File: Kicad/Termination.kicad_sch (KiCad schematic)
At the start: 29 parts, among them J1 Conn_02x25_Odd_Even, J5 Conn_02x25_Odd_Even, SW1 219-8MST, U11 DS21S07A, U12 DS21S07A, U8 SN74F244DB

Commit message: Add correct footprints for DIP resistors
And start adding LCSC part numbers
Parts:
- C1102, C1202: LCSC Part # (none) -> C7189
- J1, J5: LCSC Part # (none) -> C7494769
- R1, R2: footprint kicad-official/Resistor_SMD.pretty:R_0603_1608Metric_Pad0.98x0.95mm_HandSolder -> Resistor_SMD:R_0603_1608Metric_Pad0.98x0.95mm_HandSolder
- U11, U12: LCSC Part # (none) -> C6602097
- U8: LCSC Part # (none) -> C543080
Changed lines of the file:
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@@
 			)
 		)
+		(property "LCSC Part #" "C6602097"
+			(at 40.64 54.61 0)
+			(effects
+				(font
+					(size 1.27 1.27)
+				)
+				(hide yes)
+			)
+		)
 		(pin "1"
 		)
@@
 			)
 		)
-		(property "Footprint" "kicad-official/Resistor_SMD.pretty:R_0603_1608Metric_Pad0.98x0.95mm_HandSolder"
+		(property "Footprint" "Resistor_SMD:R_0603_1608Metric_Pad0.98x0.95mm_HandSolder"
 			(at 88.9 151.13 0)
 			(effects
@@
 			)
 		)
-		(property "Footprint" "kicad-official/Resistor_SMD.pretty:R_0603_1608Metric_Pad0.98x0.95mm_HandSolder"
+		(property "Footprint" "Resistor_SMD:R_0603_1608Metric_Pad0.98x0.95mm_HandSolder"
 			(at 95.25 154.94 0)
 			(effects
@@
 			)
 		)
+		(property "LCSC Part #" "C6602097"
+			(at 40.64 20.32 0)
+			(effects
+				(font
+					(size 1.27 1.27)
+				)
+				(hide yes)
+			)
+		)
 		(pin "1"
 		)
@@
 			)
 		)
+		(property "LCSC Part #" "C7189"
+			(at 26.67 48.26 0)
+			(effects
+				(font
+					(size 1.27 1.27)
+				)
+				(hide yes)
+			)
+		)
 		(pin "1"
 		)
@@
 			)
 		)
+		(property "LCSC Part #" "C7189"
+			(at 26.67 82.55 0)
+			(effects
+				(font
+					(size 1.27 1.27)
+				)
+				(hide yes)
+			)
+		)
 		(pin "1"
 		)
@@
 			)
 		)
+		(property "LCSC Part #" "C543080"
+			(at 24.13 115.57 0)
+			(effects
+				(font
+					(size 1.27 1.27)
+				)
+				(hide yes)
+			)
+		)
 		(pin "3"
 		)
@@
 			)
 		)
+		(property "LCSC Part #" "C7494769"
+			(at 270.51 81.28 90)
+			(effects
+				(font
+					(size 1.27 1.27)
+				)
+				(hide yes)
+			)
+		)
 		(pin "1"
 		)
@@
 			(effects
 				(font
+					(size 1.27 1.27)
+				)
+				(hide yes)
+			)
+		)
+		(property "LCSC Part #" "C7494769"
+			(at 127 34.29 90)
+			(effects
+				(font

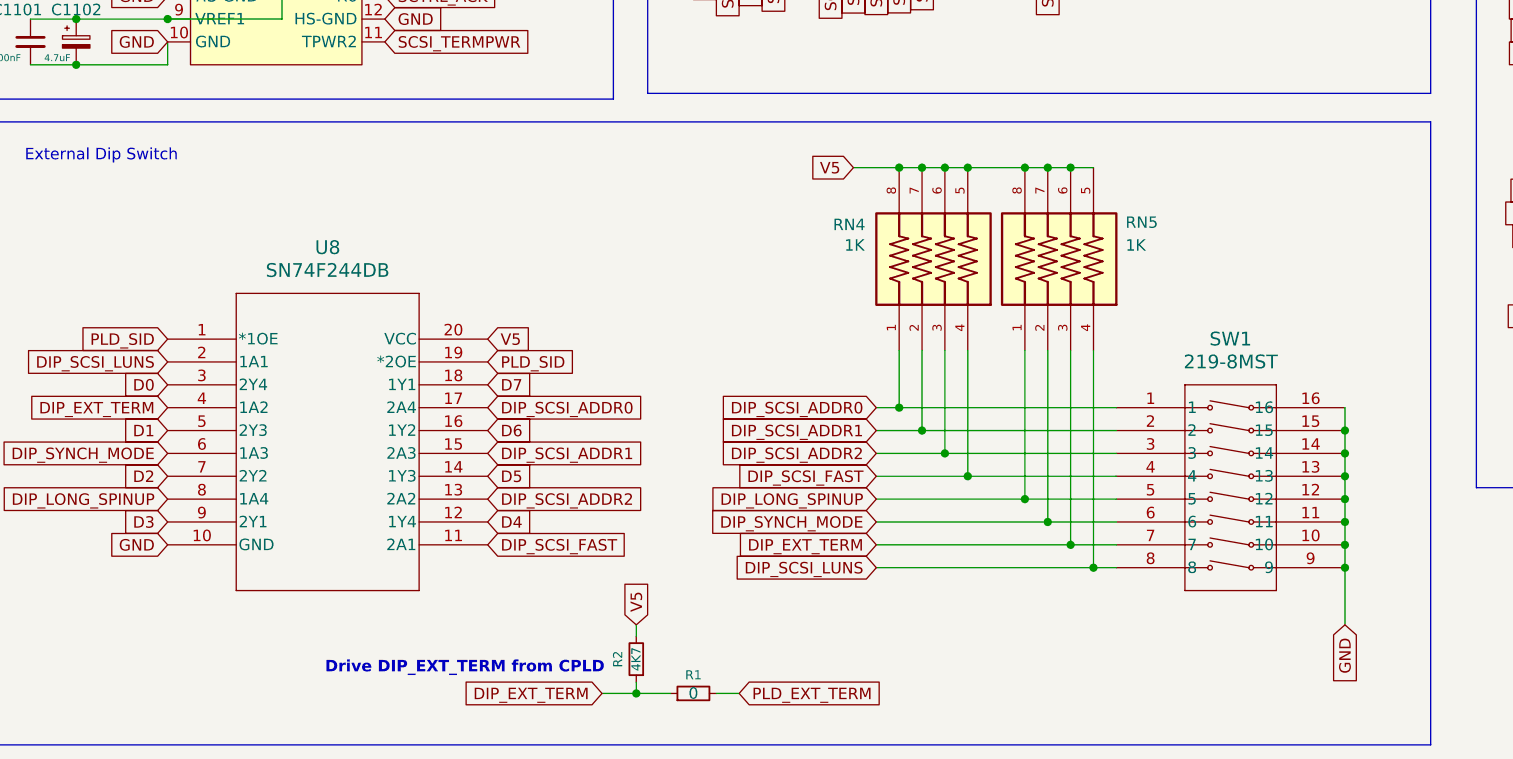
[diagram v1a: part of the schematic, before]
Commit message: Add more LCSC parts and mark some parts DNP
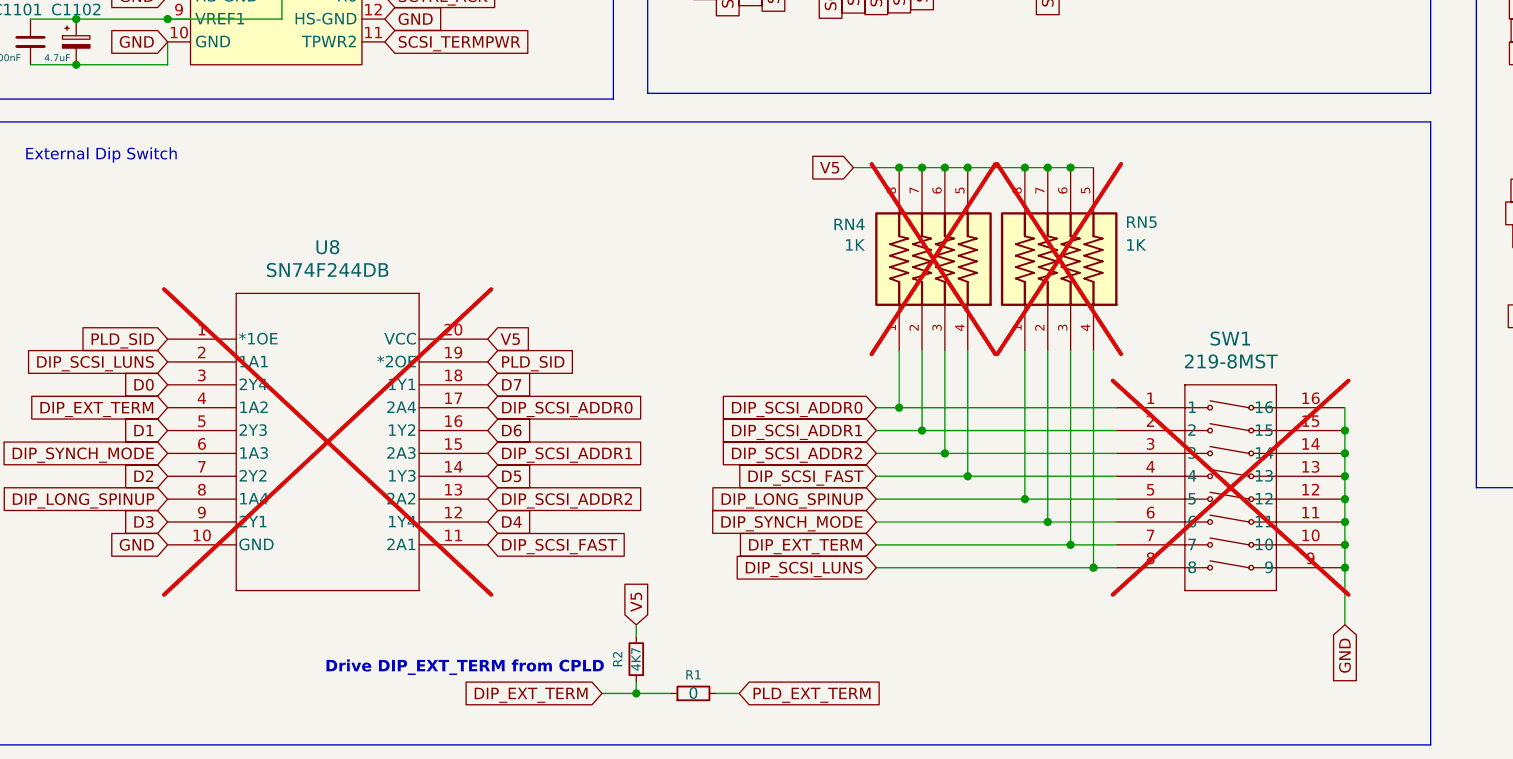
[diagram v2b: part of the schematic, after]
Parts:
- C1101, C1201: LCSC Part # (none) -> C14663
- FL1, FL10, FL2, FL3, FL4, FL5, FL6, FL7, FL8, FL9: LCSC Part # (none) -> C2662010
- RN4, RN5: LCSC Part # (none) -> C784824; now not fitted
- SW1, U8: now not fitted
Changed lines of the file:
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@@
 		(in_bom yes)
 		(on_board yes)
-		(dnp no)
+		(dnp yes)
 		(property "Reference" "RN4"
 			(at 110.744 102.87 90)
@@
 			)
 		)
+		(property "LCSC Part #" "C784824"
+			(at 123.19 106.68 90)
+			(effects
+				(font
+					(size 1.27 1.27)
+				)
+				(hide yes)
+			)
+		)
 		(pin "1"
 		)
@@
 			)
 		)
+		(property "LCSC Part #" "C2662010"
+			(at 107.95 59.69 90)
+			(effects
+				(font
+					(size 1.27 1.27)
+				)
+				(hide yes)
+			)
+		)
 		(pin "1"
 		)
@@
 			)
 		)
+		(property "LCSC Part #" "C2662010"
+			(at 205.74 87.63 90)
+			(effects
+				(font
+					(size 1.27 1.27)
+				)
+				(hide yes)
+			)
+		)
 		(pin "1"
 		)
@@
 			)
 		)
+		(property "LCSC Part #" ""
+			(at 242.57 80.01 90)
+			(effects
+				(font
+					(size 1.27 1.27)
+				)
+				(hide yes)
+			)
+		)
 		(pin "8"
 		)
@@
 			)
 		)
+		(property "LCSC Part #" ""
+			(at 88.9 151.13 90)
+			(effects
+				(font
+					(size 1.27 1.27)
+				)
+				(hide yes)
+			)
+		)
 		(pin "2"
 		)
@@
 			)
 		)
+		(property "LCSC Part #" "C2662010"
+			(at 205.74 110.49 90)
+			(effects
+				(font
+					(size 1.27 1.27)
+				)
+				(hide yes)
+			)
+		)
 		(pin "1"
 		)
@@
 		(in_bom yes)
 		(on_board yes)
-		(dnp no)
+		(dnp yes)
 		(property "Reference" "RN5"
 			(at 143.256 102.616 90)
@@
 			)
 		)
+		(property "LCSC Part #" "C784824"
+			(at 137.16 106.68 90)
+			(effects
+				(font
+					(size 1.27 1.27)
+				)
+				(hide yes)
+			)
+		)
 		(pin "1"
 		)
@@
 			)
 		)
+		(property "LCSC Part #" ""
+			(at 95.25 154.94 90)
+			(effects
+				(font
+					(size 1.27 1.27)
+				)
+				(hide yes)
+			)
+		)
 		(pin "2"
 		)
@@
 			)
 		)
+		(property "LCSC Part #" ""
+			(at 240.03 118.11 90)
+			(effects
+				(font
+					(size 1.27 1.27)
+				)
+				(hide yes)
+			)
+		)
 		(pin "7"
 		)
@@
 			)
 		)
+		(property "LCSC Part #" "C14663"
+			(at 21.59 82.55 0)
+			(effects
+				(font
+					(size 1.27 1.27)
+				)
+				(hide yes)
+			)
+		)
 		(pin "2"
 		)
@@
 		(in_bom yes)
 		(on_board yes)
-		(dnp no)
+		(dnp yes)
 		(fields_autoplaced yes)
 		(property "Reference" "SW1"
@@
 			)
 		)
+		(property "LCSC Part #" ""
+			(at 142.24 123.19 0)
+			(effects
+				(font
+					(size 1.27 1.27)
+				)
+				(hide yes)
+			)
+		)
 		(pin "3"
 		)
@@
 			)
 		)
+		(property "LCSC Part #" "C2662010"
+			(at 205.74 124.46 90)
+			(effects
+				(font
+					(size 1.27 1.27)
+				)
+				(hide yes)
+			)
+		)
 		(pin "7"
 		)
@@
 			)
 		)
+		(property "LCSC Part #" ""
+			(at 224.79 38.1 90)
+			(effects
+				(font
+					(size 1.27 1.27)
+				)
+				(hide yes)
+			)
+		)
 		(pin "2"
 		)
@@
 			)
 		)
+		(property "LCSC Part #" "C2662010"
+			(at 146.05 59.69 90)
+			(effects
+				(font
+					(size 1.27 1.27)
+				)
+				(hide yes)
+			)
+		)
 		(pin "1"
 		)
@@
 			)
 		)
+		(property "LCSC Part #" "C2662010"
+			(at 121.92 59.69 90)
+			(effects
+				(font
+					(size 1.27 1.27)
+				)
+				(hide yes)
+			)
+		)
 		(pin "7"
 		)
@@
 			)
 		)
+		(property "LCSC Part #" ""
+			(at 237.49 38.1 90)
+			(effects
+				(font
+					(size 1.27 1.27)
+				)
+				(hide yes)
+			)
+		)
 		(pin "5"
 		)
@@
 			)
 		)
+		(property "LCSC Part #" "C2662010"
+			(at 205.74 58.42 90)
+			(effects
+				(font
+					(size 1.27 1.27)
+				)
+				(hide yes)
+			)
+		)
 		(pin "1"
 		)
@@
 		(in_bom yes)
 		(on_board yes)
-		(dnp no)
+		(dnp yes)
 		(fields_autoplaced yes)
 		(property "Reference" "U8"
@@
 			)
 		)
+		(property "LCSC Part #" "C14663"
+			(at 21.59 48.26 0)
+			(effects
+				(font
+					(size 1.27 1.27)
+				)
+				(hide yes)
+			)
+		)
 		(pin "2"
 		)
@@
 			)
 		)
+		(property "LCSC Part #" "C2662010"
+			(at 173.99 59.69 90)
+			(effects
+				(font
+					(size 1.27 1.27)
+				)
+				(hide yes)
+			)
+		)
 		(pin "1"
 		)
@@
 			)
 		)
+		(property "LCSC Part #" "C2662010"
+			(at 160.02 59.69 90)
+			(effects
+				(font
+					(size 1.27 1.27)
+				)
+				(hide yes)
+			)
+		)
 		(pin "7"
 		)
@@
 			)
 		)
+		(property "LCSC Part #" "C2662010"
+			(at 205.74 72.39 90)
+			(effects
+				(font
+					(size 1.27 1.27)
+				)
+				(hide yes)
+			)
+		)
 		(pin "7"
 		)
@@
 			(effects
 				(font
+					(size 1.27 1.27)
+				)
+				(hide yes)
+			)
+		)
+		(property "LCSC Part #" ""
+			(at 242.57 118.11 90)
+			(effects
+				(font

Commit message: RN15 pin swap
As requested in issue #7
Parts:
- C10, C6, C7, C8, C9: LCSC Part # (none) -> C576629
- R1: LCSC Part # (none) -> C95177
- R2: LCSC Part # (none) -> C99782
- SW1: LCSC Part # (none) -> C2842674

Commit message: Update SCSI connector
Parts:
- J1, J5: LCSC Part # C7494769 -> C221059
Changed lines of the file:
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@@
 			)
 		)
-		(property "LCSC Part #" "C7494769"
+		(property "LCSC Part #" "C221059 "
 			(at 270.51 81.28 90)
 			(effects
@@
 			)
 		)
-		(property "LCSC Part #" "C7494769"
+		(property "LCSC Part #" "C221059 "
 			(at 127 34.29 90)
 			(effects

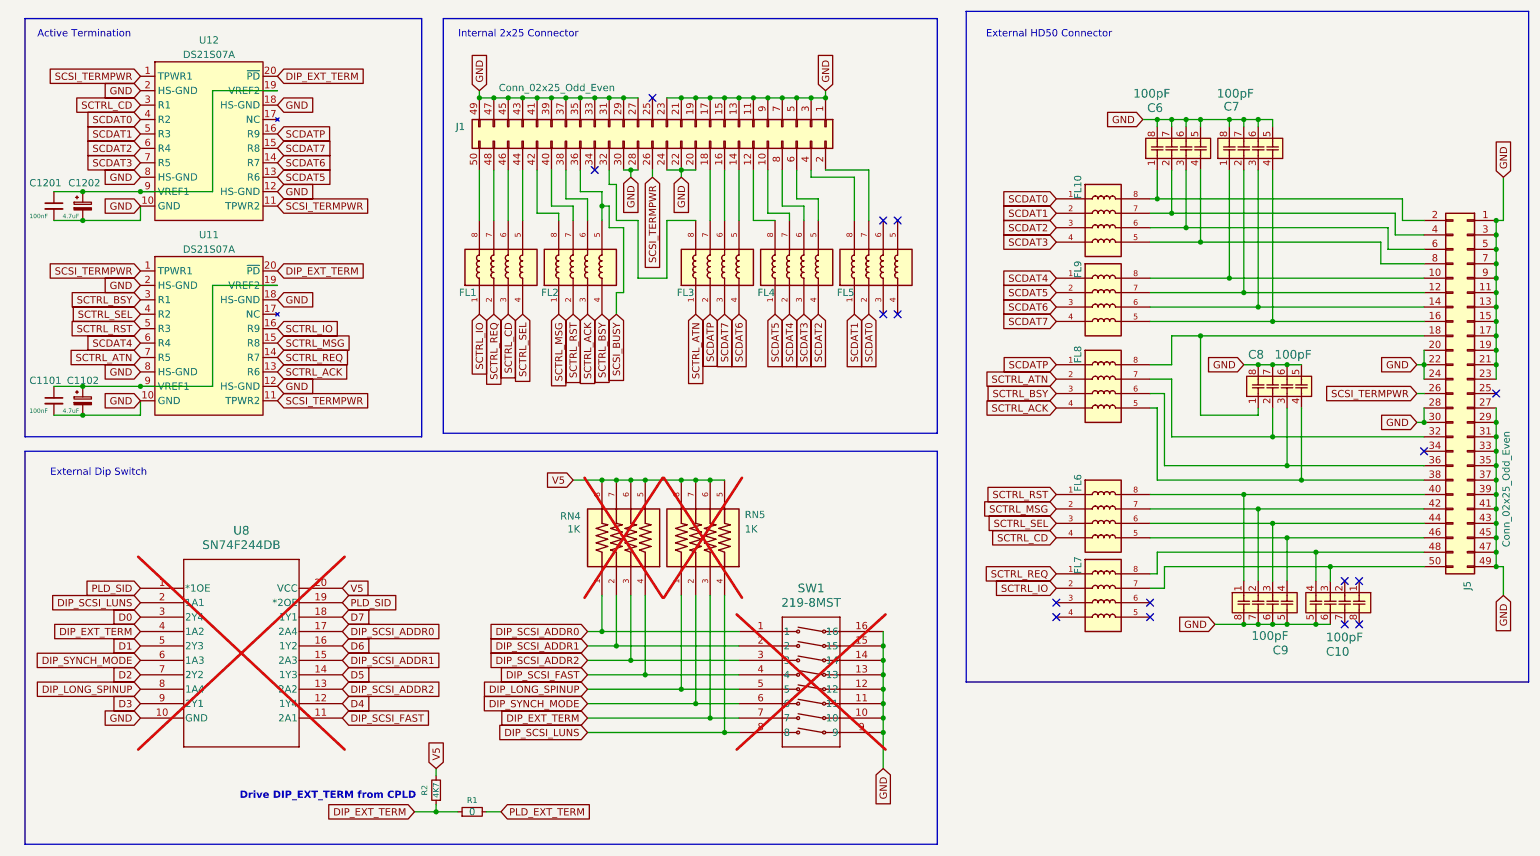
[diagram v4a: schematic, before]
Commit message: Add fiducials and clean up schematics
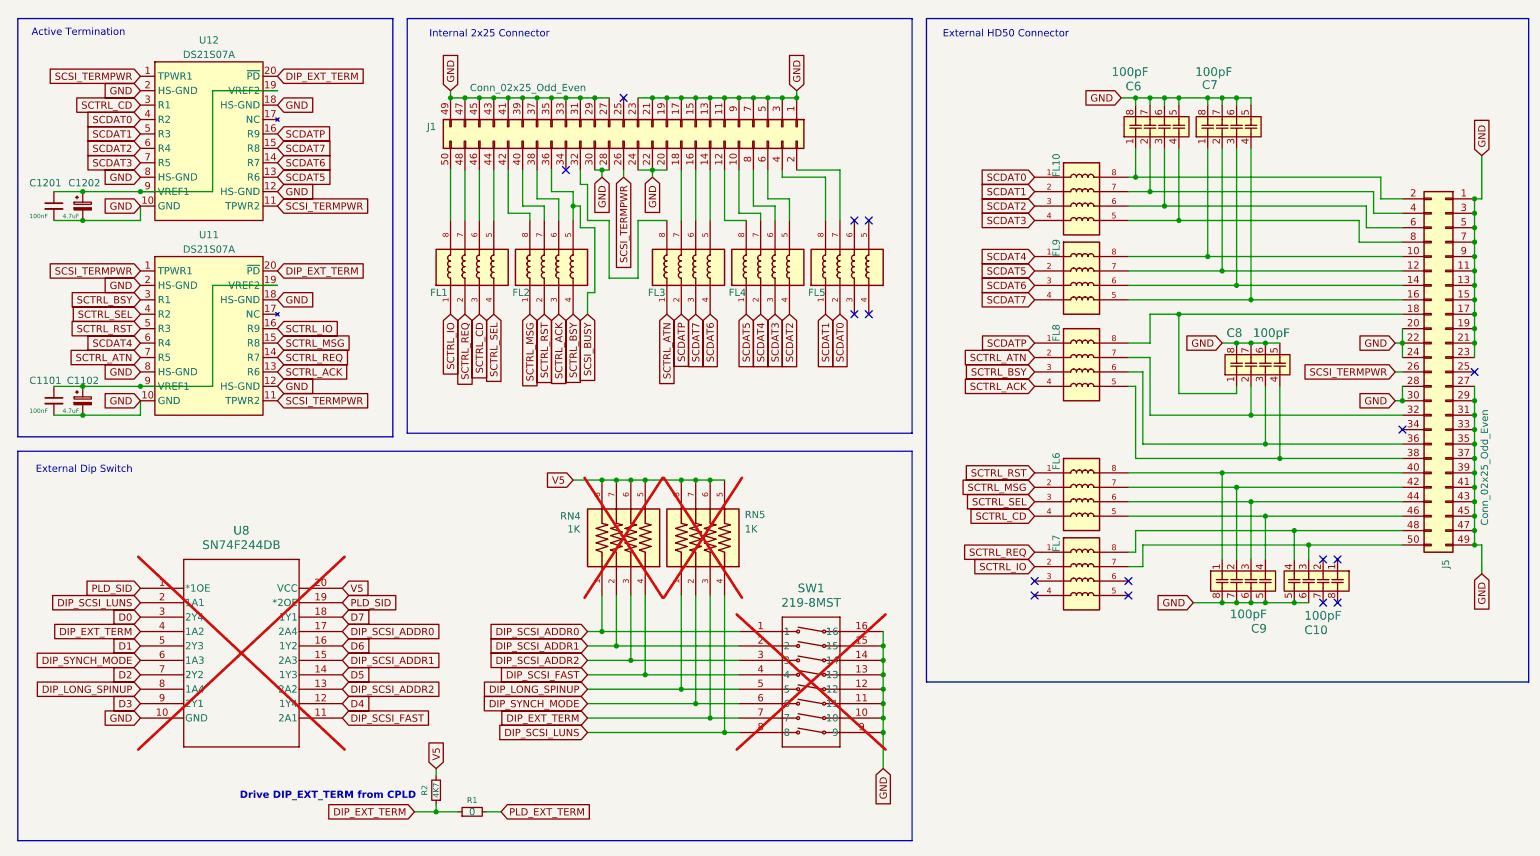
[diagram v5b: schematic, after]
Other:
- moved on the sheet: C10, C6, C7, C8, C9, FL1, FL10, FL2, FL3, FL4, FL5, FL6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
